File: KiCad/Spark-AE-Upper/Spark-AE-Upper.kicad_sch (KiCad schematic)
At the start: 0 parts

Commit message: filled in title blocks
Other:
- company: (none) -> Copyright © 2025 clectric.diy Licensed under CERN-OHL-S v2
- title: (none) -> Spark-AE-Upper
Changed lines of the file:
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@@
 	(generator_version "9.0")
 	(paper "A4")
+	(title_block
+		(title "Spark-AE-Upper")
+		(date "2026-01-14")
+		(rev "0.1")
+		(company "Copyright © 2025 clectric.diy Licensed under CERN-OHL-S v2")
+		(comment 1 "Charles H. Leggett")
+	)
 	(sheet_instances
 		(path "/"

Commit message: bumping copyright year
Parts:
- added RP1, RP2: RK09K1130D62, easyeda2kicad:RES-TH_RK09K1130AAU, symbol easyeda2kicad:RK09K1130D62
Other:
- company: Copyright © 2025 clectric.diy Licensed under CERN-OHL-S v2 -> Copyright © 2026 clectric.diy Licensed under CERN-OHL-S v2
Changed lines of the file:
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@@
 		(date "2026-01-14")
 		(rev "0.1")
-		(company "Copyright © 2025 clectric.diy Licensed under CERN-OHL-S v2")
+		(company "Copyright © 2026 clectric.diy Licensed under CERN-OHL-S v2")
 		(comment 1 "Charles H. Leggett")
 	)
+	(symbol
+		(lib_id "easyeda2kicad:RK09K1130D62")
+		(at 123.19 81.28 0)
+		(unit 1)
+		(exclude_from_sim no)
+		(in_bom yes)
+		(on_board yes)
+		(dnp no)
+		(fields_autoplaced yes)
+		(property "Reference" "RP2"
+			(at 123.695 86.36 0)
+			(effects
+				(font
+					(size 1.27 1.27)
+				)
+			)
+		)
+		(property "Value" "RK09K1130D62"
+			(at 123.695 88.9 0)
+			(effects
+				(font
+					(size 1.27 1.27)
+				)
+			)
+		)
+		(property "Footprint" "easyeda2kicad:RES-TH_RK09K1130AAU"
+			(at 123.19 91.95 0)
+			(effects
+				(font
+					(size 1.27 1.27)
+				)
+				(hide yes)
+			)
+		)
+		(property "Datasheet" ""
+			(at 123.19 81.28 0)
+			(effects
+				(font
+					(size 1.27 1.27)
+				)
+				(hide yes)
+			)
+		)
+		(property "Description" ""
+			(at 123.19 81.28 0)
+			(effects
+				(font
+					(size 1.27 1.27)
+				)
+				(hide yes)
+			)
+		)
+		(property "LCSC Part" "C470399"
+			(at 123.19 94.49 0)
+			(effects
+				(font
+					(size 1.27 1.27)
+				)
+				(hide yes)
+			)
+		)
+		(pin "5"
+		)
+		(pin "2"
+		)
+		(pin "1"
+		)
+		(pin "3"
+		)
+		(pin "4"
+		)
+		(instances
+			(project "Spark-AE-Upper"
+				(path "/b249adcd-2848-4e56-9615-c4f1b6083abe"
+					(reference "RP2")
+					(unit 1)
+				)
+			)
+		)
+	)
+	(symbol
+		(lib_id "easyeda2kicad:RK09K1130D62")
+		(at 99.06 81.28 0)
+		(unit 1)
+		(exclude_from_sim no)
+		(in_bom yes)
+		(on_board yes)
+		(dnp no)
+		(fields_autoplaced yes)
+		(property "Reference" "RP1"
+			(at 99.565 86.36 0)
+			(effects
+				(font
+					(size 1.27 1.27)
+				)
+			)
+		)
+		(property "Value" "RK09K1130D62"
+			(at 99.565 88.9 0)
+			(effects
+				(font
+					(size 1.27 1.27)
+				)
+			)
+		)
+		(property "Footprint" "easyeda2kicad:RES-TH_RK09K1130AAU"
+			(at 99.06 91.95 0)
+			(effects
+				(font
+					(size 1.27 1.27)
+				)
+				(hide yes)
+			)
+		)
+		(property "Datasheet" ""
+			(at 99.06 81.28 0)
+			(effects
+				(font
+					(size 1.27 1.27)
+				)
+				(hide yes)
+			)
+		)
+		(property "Description" ""
+			(at 99.06 81.28 0)
+			(effects
+				(font
+					(size 1.27 1.27)
+				)
+				(hide yes)
+			)
+		)
+		(property "LCSC Part" "C470399"
+			(at 99.06 94.49 0)
+			(effects
+				(font
+					(size 1.27 1.27)
+				)
+				(hide yes)
+			)
+		)
+		(pin "5"
+		)
+		(pin "2"
+		)
+		(pin "1"
+		)
+		(pin "3"
+		)
+		(pin "4"
+		)
+		(instances
+			(project ""
+				(path "/b249adcd-2848-4e56-9615-c4f1b6083abe"
+					(reference "RP1")
+					(unit 1)
+				)
+			)
+		)
+	)
 	(sheet_instances

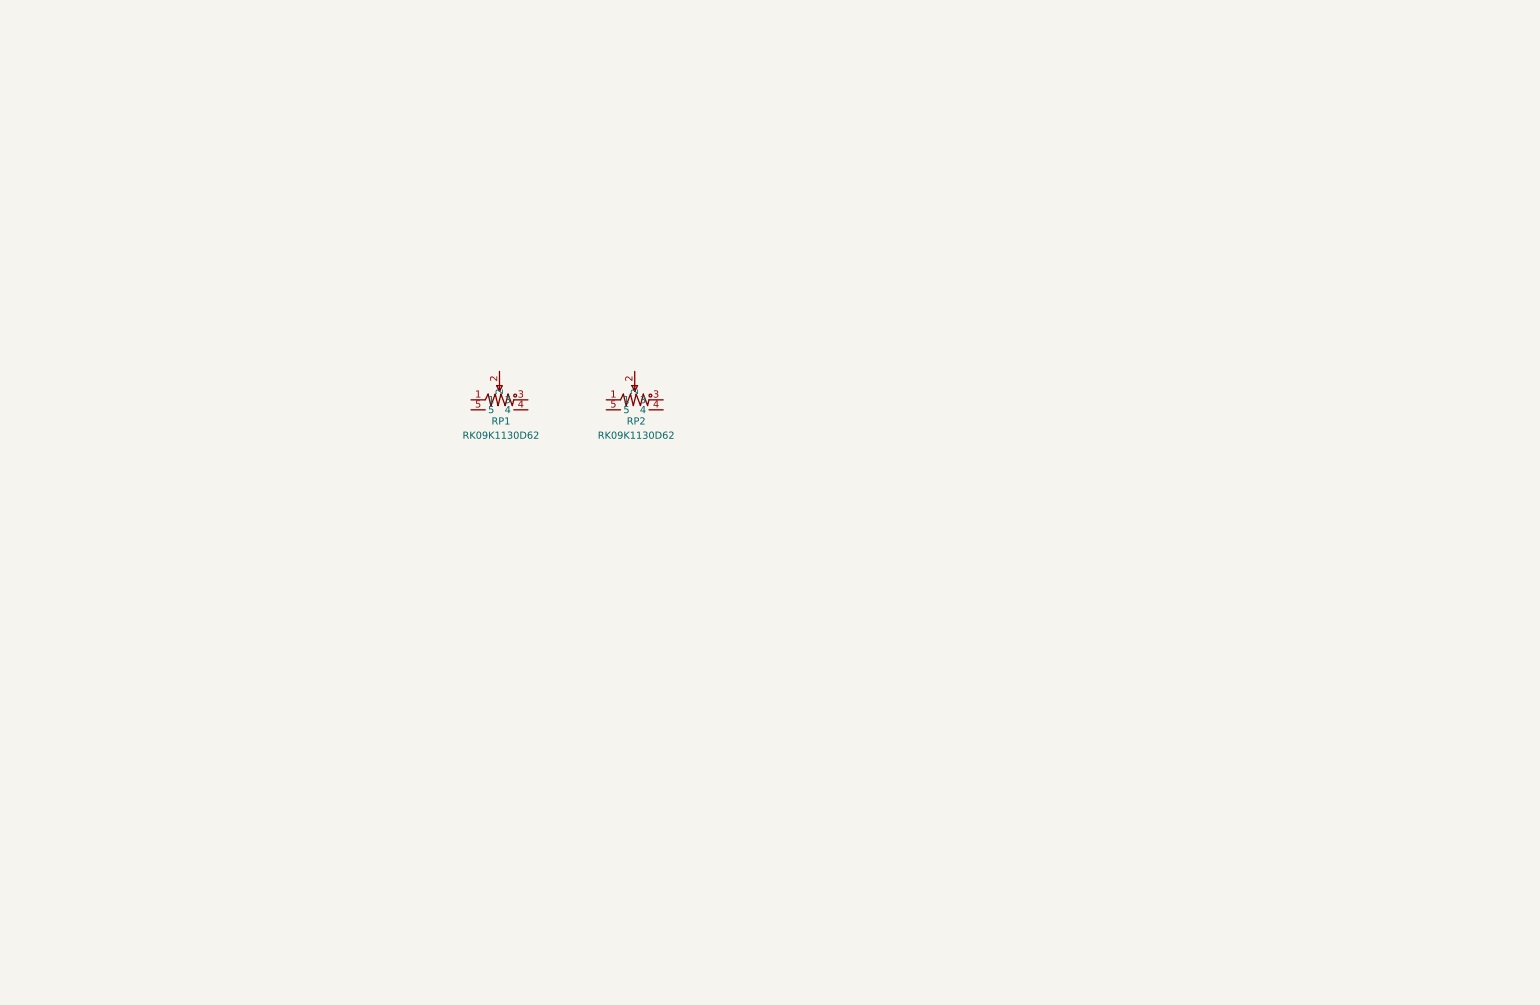
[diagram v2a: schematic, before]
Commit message: laid out upper board interface and connections
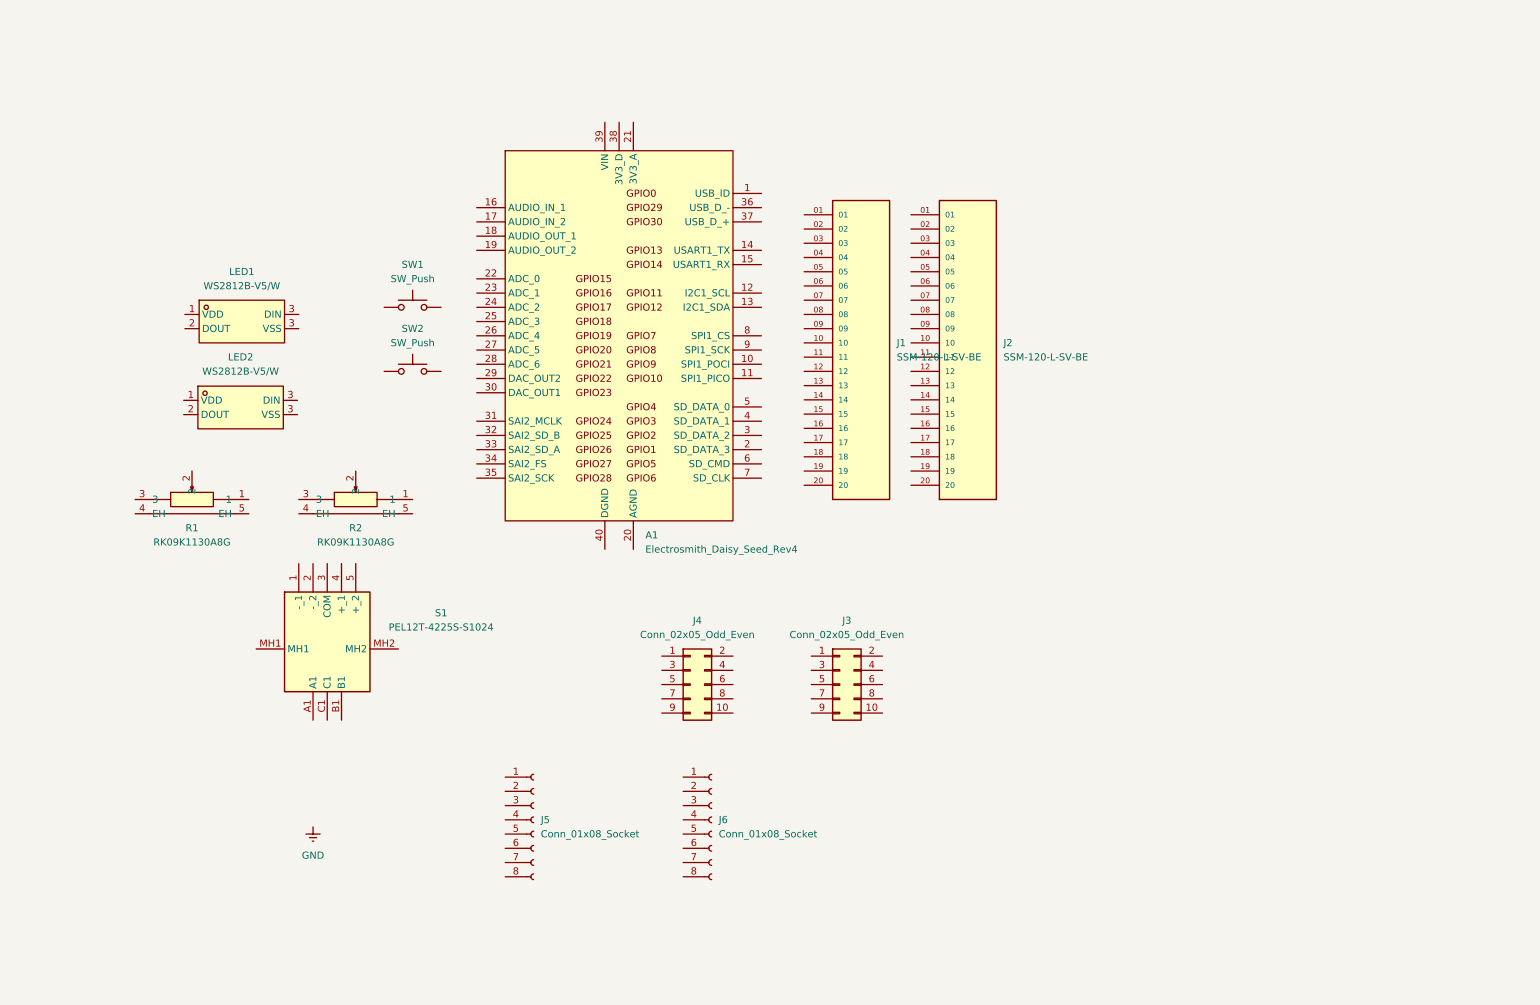
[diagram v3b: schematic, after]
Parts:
- removed RP1, RP2: RK09K1130D62, easyeda2kicad:RES-TH_RK09K1130AAU, symbol easyeda2kicad:RK09K1130D62
- added A1: Electrosmith_Daisy_Seed_Rev4, Module:Electrosmith_Daisy_Seed, symbol MCU_Module:Electrosmith_Daisy_Seed_Rev4
- added J1, J2: SSM-120-L-SV-BE, clectric-diy:SAMTEC_SSM-120-L-SV-BE, symbol clectric-diy:SSM-120-L-SV-BE
- added J3, J4: Conn_02x05_Odd_Even, Connector_PinHeader_2.54mm:PinHeader_2x05_P2.54mm_Vertical, symbol Connector_Generic:Conn_02x05_Odd_Even
- added J5, J6: Conn_01x08_Socket, Connector_PinSocket_2.54mm:PinSocket_1x08_P2.54mm_Vertical, symbol Connector:Conn_01x08_Socket
- added LED1, LED2: WS2812B-V5/W, clectric-diy:LED-SMD_4P-L5.0-W5.0-TL-1, symbol clectric-diy:WS2812B-V5_W
- added R1, R2: RK09K1130A8G, clectric-diy:RES-TH_RK09K113004U, symbol clectric-diy:RK09K1130A8G
- added S1: PEL12T-4225S-S1024, PEL12T4225SS1024, symbol clectric-diy:PEL12T-4225S-S1024
- added SW1, SW2: SW_Push, Button_Switch_THT:SW_PUSH_6mm, symbol Switch:SW_Push

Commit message: added and connected nets for daisy seed socket
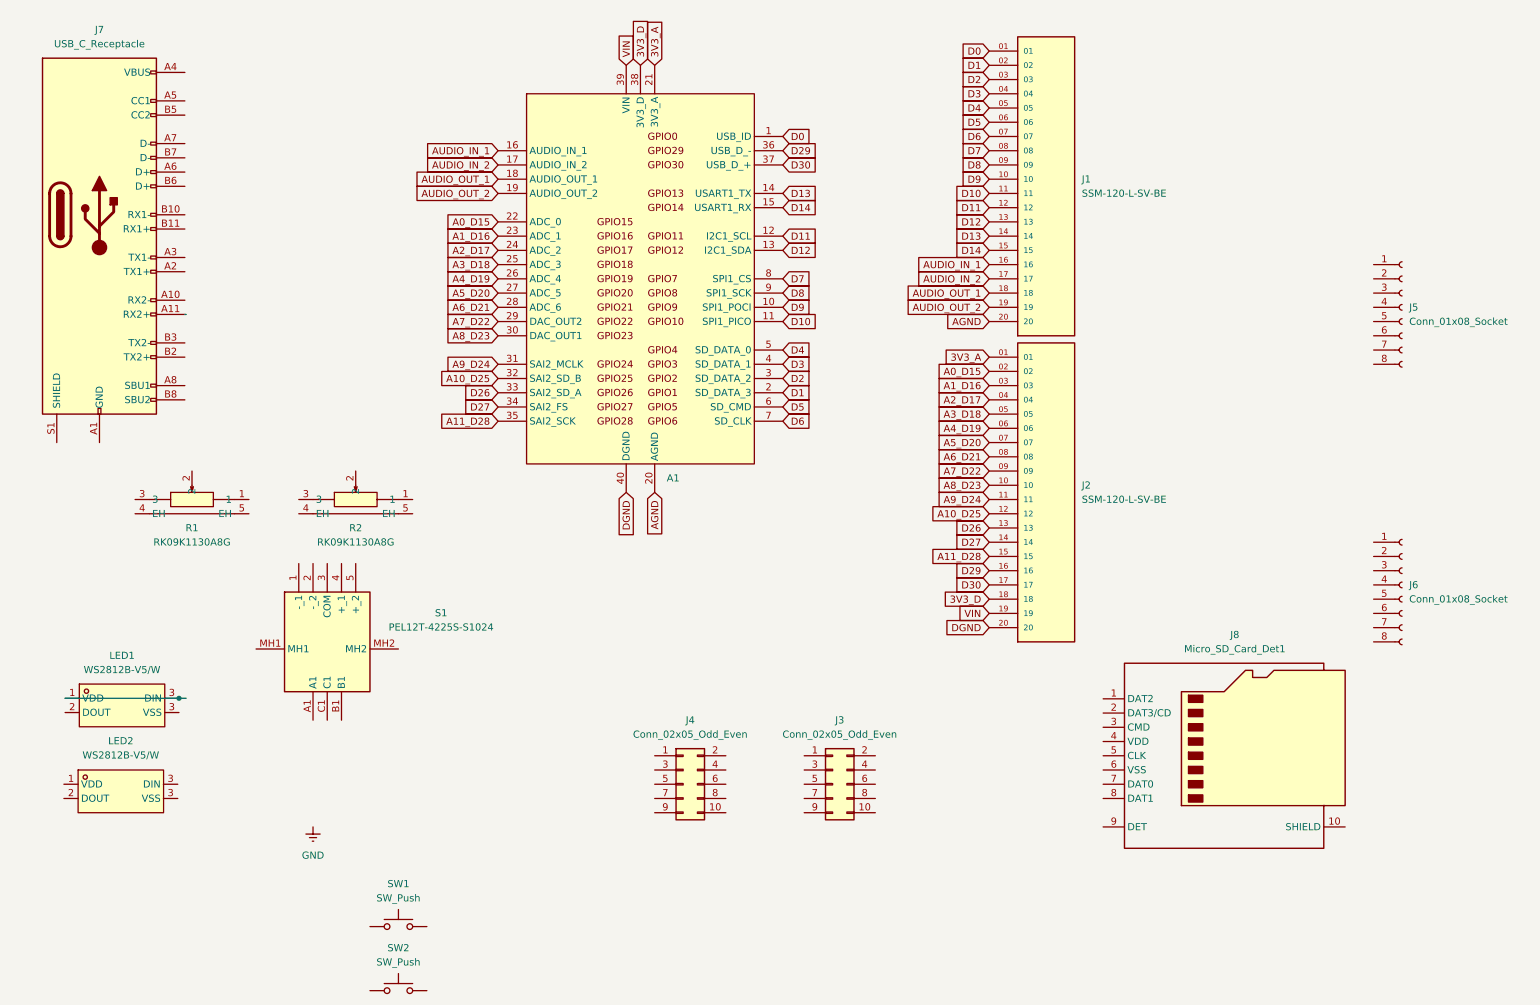
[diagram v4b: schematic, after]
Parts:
- added J7: USB_C_Receptacle, Connector_USB:USB_C_Receptacle_GCT_USB4105-xx-A_16P_TopMnt_Horizontal, symbol Connector:USB_C_Receptacle
- added J8: Micro_SD_Card_Det1, Connector_Card:microSD_HC_Molex_104031-0811, symbol Connector:Micro_SD_Card_Det1
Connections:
- net at LED1.1 (VDD): now also LED1.3 (VSS)
- net D0: now reaches A1.1 (USB_ID)
- net D0: now also J1.01
- net D9: now reaches A1.10 (SPI1_POCI)
- net D9: now also J1.10
- net D10: now reaches A1.11 (SPI1_PICO)
- net D10: now also J1.11
- net D11: now reaches A1.12 (I2C1_SCL)
- net D11: now also J1.12
- net D12: now reaches A1.13 (I2C1_SDA)
- net D12: now also J1.13
- net D13: now reaches A1.14 (USART1_TX)
- net D13: now also J1.14
- net D14: now reaches A1.15 (USART1_RX)
- net D14: now also J1.15
- net AUDIO_IN_1: now reaches A1.16 (AUDIO_IN_1)
- net AUDIO_IN_1: now also J1.16
- net AUDIO_IN_2: now reaches A1.17 (AUDIO_IN_2)
- net AUDIO_IN_2: now also J1.17
- net AUDIO_OUT_1: now reaches A1.18 (AUDIO_OUT_1)
- net AUDIO_OUT_1: now also J1.18
- net AUDIO_OUT_2: now reaches A1.19 (AUDIO_OUT_2)
- net AUDIO_OUT_2: now also J1.19
- net D1: now reaches A1.2 (SD_DATA_3)
- net D1: now also J1.02
- net AGND: now reaches A1.20 (AGND)
- net AGND: now also J1.20
- net 3V3_A: now reaches A1.21 (3V3_A)
- net 3V3_A: now also J2.01
- net A0_D15: now reaches A1.22 (ADC_0)
- net A0_D15: now also J2.02
- net A1_D16: now reaches A1.23 (ADC_1)
- net A1_D16: now also J2.03
- net A2_D17: now reaches A1.24 (ADC_2)
- net A2_D17: now also J2.04
- net A3_D18: now reaches A1.25 (ADC_3)
- net A3_D18: now also J2.05
- net A4_D19: now reaches A1.26 (ADC_4)
- net A4_D19: now also J2.06
- net A5_D20: now reaches A1.27 (ADC_5)
- net A5_D20: now also J2.07
- net A6_D21: now reaches A1.28 (ADC_6)
- net A6_D21: now also J2.08
- net A7_D22: now reaches A1.29 (DAC_OUT2)
- net A7_D22: now also J2.09
- net D2: now reaches A1.3 (SD_DATA_2)
- net D2: now also J1.03
- net A8_D23: now reaches A1.30 (DAC_OUT1)
- net A8_D23: now also J2.10
- net A9_D24: now reaches A1.31 (SAI2_MCLK)
- net A9_D24: now also J2.11
- net A10_D25: now reaches A1.32 (SAI2_SD_B)
- net A10_D25: now also J2.12
- net D26: now reaches A1.33 (SAI2_SD_A)
- net D26: now also J2.13
- net D27: now reaches A1.34 (SAI2_FS)
- net D27: now also J2.14
- net A11_D28: now reaches A1.35 (SAI2_SCK)
- net A11_D28: now also J2.15
- net D29: now reaches A1.36 (USB_D_-)
- net D29: now also J2.16
- net D30: now reaches A1.37 (USB_D_+)
- net D30: now also J2.17
- net 3V3_D: now reaches A1.38 (3V3_D)
- net 3V3_D: now also J2.18
- net VIN: now reaches A1.39 (VIN)
- net VIN: now also J2.19
- net D3: now reaches A1.4 (SD_DATA_1)
- net D3: now also J1.04
- net DGND: now reaches A1.40 (DGND)
- net DGND: now also J2.20
- net D4: now reaches A1.5 (SD_DATA_0)
- net D4: now also J1.05
- net D5: now reaches A1.6 (SD_CMD)
- net D5: now also J1.06
- net D6: now reaches A1.7 (SD_CLK)
- net D6: now also J1.07
- net D7: now reaches A1.8 (SPI1_CS)
- net D7: now also J1.08
- net D8: now reaches A1.9 (SPI1_SCK)
- net D8: now also J1.09
- new net: J7.A1 (GND), J7.A12 (GND), J7.B1 (GND), J7.B12 (GND)
- new net: J7.A4 (VBUS), J7.A9 (VBUS), J7.B4 (VBUS), J7.B9 (VBUS)
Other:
- moved on the sheet: A1, J3, J4, J5, J6, LED1, LED2, SW1, SW2
